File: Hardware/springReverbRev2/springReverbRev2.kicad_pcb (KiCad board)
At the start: 2 copper layers, 215 x 159.5 mm, 100 parts, among them IC102 TL074, IC103 TL074, J901 AudioJack2_SwitchT, J902 AudioJack2, J903 AudioJack2, J904 AudioJack2, J905 AudioJack2_SwitchT, J906 AudioJack2, J907 Conn_01x08_Socket, J908 Conn_01x08_Pin, J909 Conn_01x09_Socket, J910 Conn_01x09_Pin, J911 2_pin_Molex_header, J912 2_pin_Molex_header, SW901 SW_SPDT_MSM, U1 TL072, U2 TL072, U7 NE5532, U901 L78L05_TO92, X101 RCA, X102 RCA

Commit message: PCB revisions, Docs
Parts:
- added B901: Board, AO_tht:Board_Marker, F.Cu at (182.0, 28.5)
- added B902: Board, AO_tht:Board_Marker, F.Cu at (141.0, 28.5)
- C1, C101, C109, C2: footprint AO_tht:C_Disc_D3.0mm_W1.6mm_P2.50mm -> AO_tht:C_Radial_D8.0mm_H11.5mm_P3.50mm
- C108, C110, C3, C4: footprint AO_tht:C_Disc_D3.0mm_W1.6mm_P2.50mm -> AO_tht:C_Rect_L7.2mm_W2.5mm_P5.00mm_FKS2_FKP2_MKS2_MKP2
- moved C109 11.5 mm to (195.2, 117.8), turned to 180 degrees
- moved C110 5.12 mm to (194.0, 105.1)
- moved X101 3.38 mm to (247.3, 118.2)
- moved X102 3.38 mm to (265.1, 118.2)
- moved C101 2.87 mm to (251.1, 135.2)
- moved C4 2.50 mm to (215.6, 74.5)
- moved C108 2.46 mm to (230.8, 129.3)
- moved C1 1.27 mm to (200.3, 131.8)
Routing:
- net Net-(C109-Pad1): track 8.45 -> 20.3 mm
- net Net-(IC102B--): track 27.5 -> 34.3 mm
- net /Back board/TO_TANK: track 128.0 -> 133.7 mm
- net /Back board/MIXPOT_WET_B: track 81.8 -> 84.4 mm
- net /Back board/TRIM_B: track 22.8 -> 24.7 mm
- net /Back board/TO_TANK_S_B: track 126.3 -> 128.1 mm
- net /Back board/AUDIO_IN_2: track 116.0 -> 114.3 mm
- net /Back board/IN_1: track 40.4 -> 38.8 mm
- net +12V: track 161.4 -> 162.5 mm
- net /Back board/EQ_POT_3_B: track 46.3 -> 45.3 mm
- net /Back board/EQ_POT_1_B: track 41.1 -> 42.2 mm
- net /Back board/IN_2: track 9.74 -> 8.74 mm
- net /Front board/AUDIO_IN_1: track 50.1 -> 51.1 mm
- net /Back board/XFADE: track 57.8 -> 58.7 mm
- net /Back board/REVERB_RETURN: track 111.3 -> 110.7 mm
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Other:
- board text added: "Circuit design by Tom Whitwell CC-BY-SA"
- board text added: "FROM/GND"
- board text added: "Kosmo layout by Rich Holmes Mar 2023"
- board text added: "TO/GND"
- board text added: "https://github.com/TomWhitwell/Spring-Reverb-Mk-2"
- board text removed: "Circuit design by Tom Whitwell https://github.com/TomWhitwell/Spring-Reverb-Mk-2 CC-BY-SA"
- board text removed: "Kosmo layout by Rich Holmes Feb 2022"

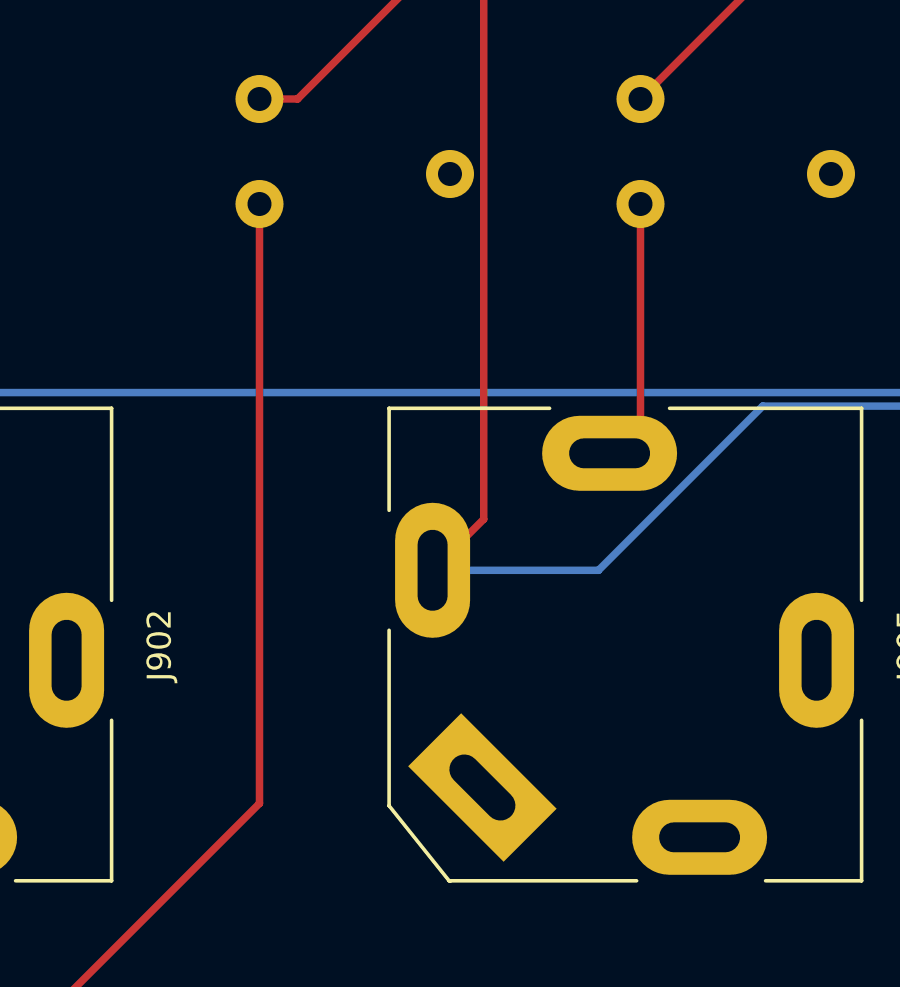
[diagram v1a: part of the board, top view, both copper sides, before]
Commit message: Restore R4 and R5 references; change C1 and C2 values; mark R5 to omit; README list of changes
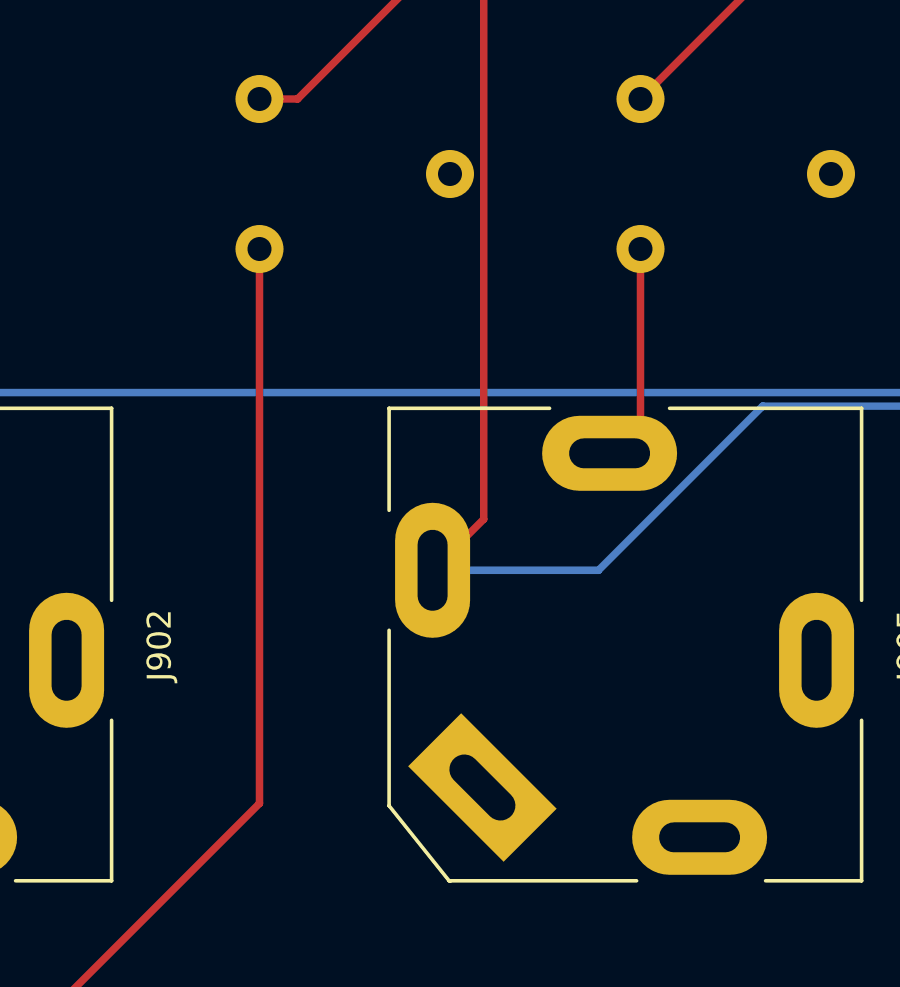
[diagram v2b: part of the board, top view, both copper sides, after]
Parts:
- C1, C2: value 10uF -> 1uF; footprint AO_tht:C_Radial_D8.0mm_H11.5mm_P3.50mm -> AO_tht:C_Rect_L7.2mm_W7.2mm_P5.00mm_FKS2_FKP2_MKS2_MKP2
- renumbered R901 to R4, R902 to R5
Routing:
- net /Back board/IN_2: track 8.74 -> 7.24 mm
- net /Back board/IN_1: track 38.8 -> 37.3 mm
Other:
- board text added: "OMIT?"

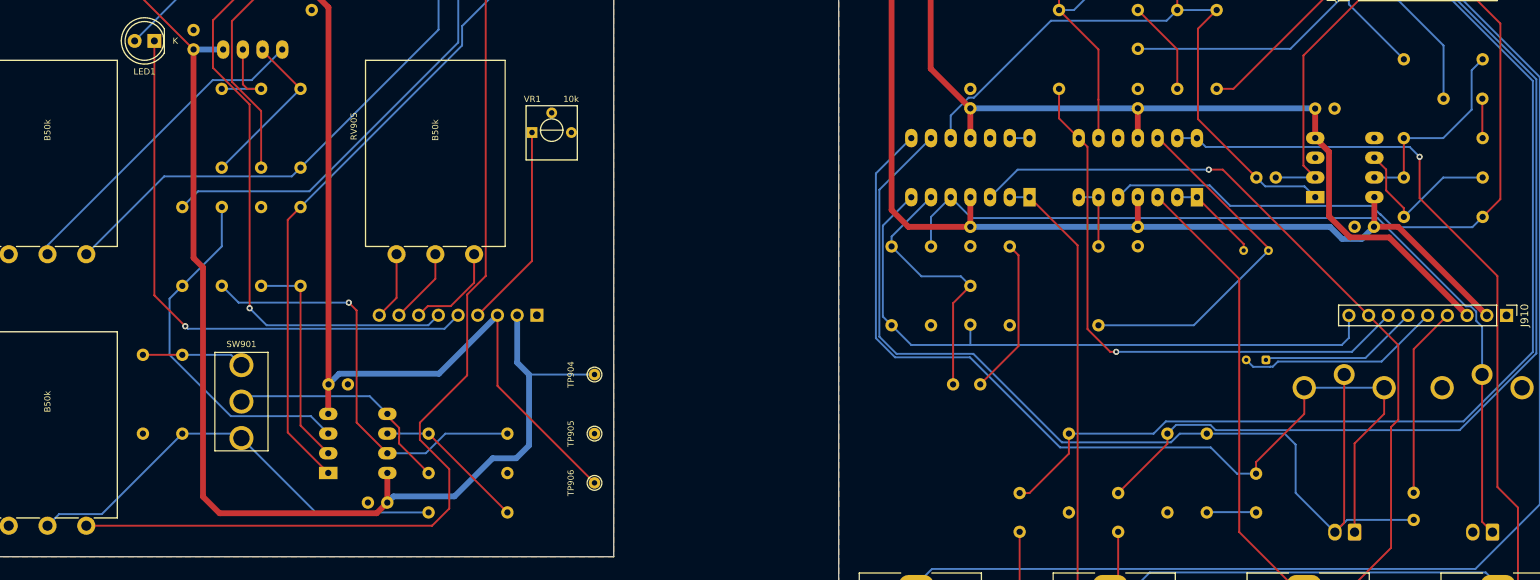
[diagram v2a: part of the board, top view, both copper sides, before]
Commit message: Docs; make LED position consistent
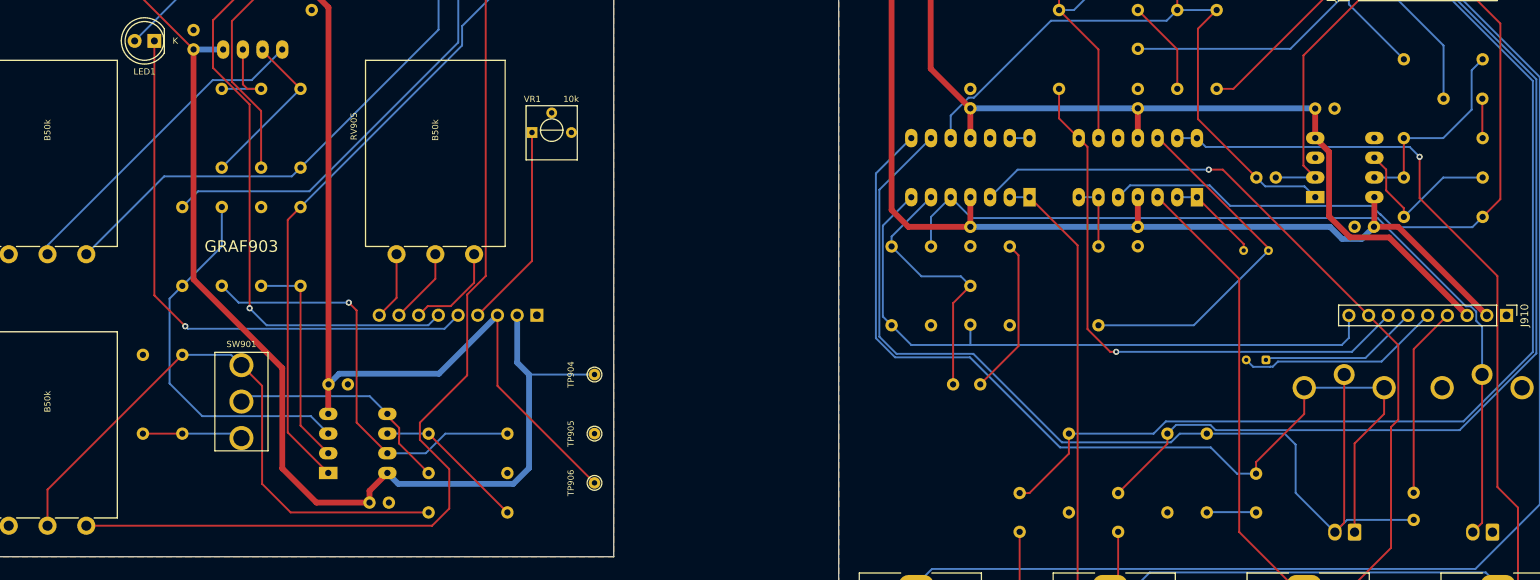
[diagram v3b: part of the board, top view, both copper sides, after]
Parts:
- added GRAF903: Holes, springreverb:springreverb_panel_holes2, F.Cu at (100.0, 100.0)
- moved R25 10.2 mm to (87.3, 124.1), turned to 90 degrees
- moved R26 10.2 mm to (92.4, 114.0), turned to -90 degrees
- moved C903 2.29 mm to (116.5, 133.0), turned to 0 degrees
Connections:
- net /Back board/MIXPOT_DRY_B renamed /Back board/MIXPOT_BRICK_B
- net /Back board/MIXPOT_WET_B renamed /Back board/MIXPOT_SPRING_B
- net /Front board/MIXPOT_DRY_F renamed /Front board/MIXPOT_BRICK_F
- net /Front board/MIXPOT_MIX_F renamed /Front board/MIXPOT_SB_MIX_F
- net /Front board/MIXPOT_WET_F renamed /Front board/MIXPOT_SPRING_F
- J907 pad 8: unconnected-(J907-Pin_8-Pad8) -> GND
- J908 pad 8: unconnected-(J908-Pin_8-Pad8) -> GND_B
- J912 pad 1: /Back board/FROM_TANK -> GND_B
- J912 pad 2: GND_B -> /Back board/FROM_TANK
- R25 pad 1: /Front board/FB_ON -> Net-(R25-Pad1)
- R26 pad 2: /Front board/FB_ON -> Net-(R25-Pad1)
- SW901 pad 1: /Front board/FB_LEVEL -> Net-(R25-Pad1)
- SW901 pad 3: /Front board/FB_ON -> /Front board/FB_LEVEL
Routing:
- net /Front board/FB_LEVEL: track 58.3 -> 76.8 mm
- net /Front board/FB_ON: track 13.3 -> 0.00 mm
- net Net-(R25-Pad1): track 0.00 -> 12.9 mm
- net +12V: track 162.5 -> 153.2 mm
- net Net-(U1A-+): track 46.5 -> 48.7 mm
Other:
- board text added: "GND/FROM"
- board text added: "Kosmo layout by Rich Holmes April 2023"
- board text added: "TO SLV/TIP"
- board text removed: "FROM/GND"
- board text removed: "Kosmo layout by Rich Holmes Mar 2023"
- board text removed: "TO/GND"

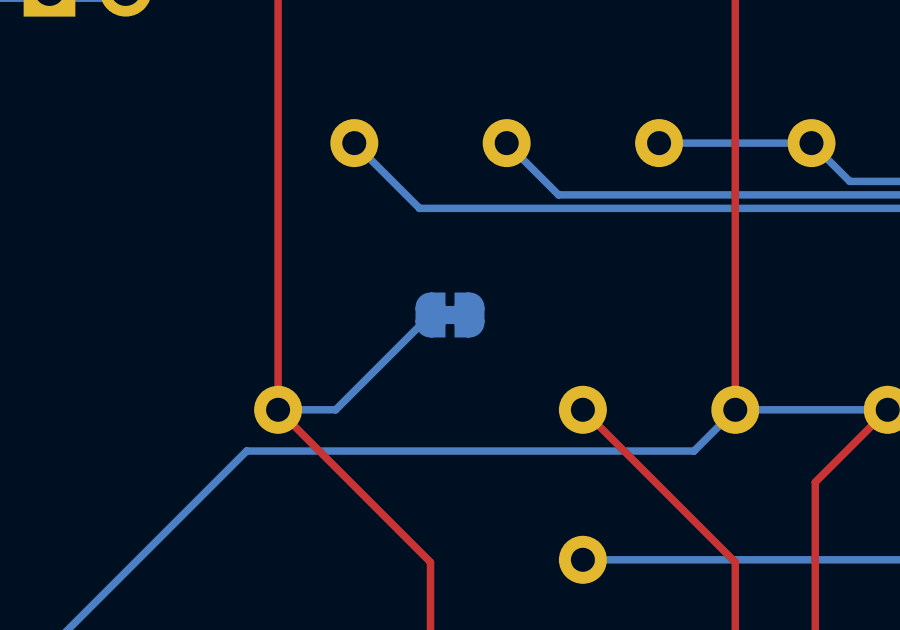
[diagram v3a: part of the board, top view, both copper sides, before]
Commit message: Use open not bridged jumper
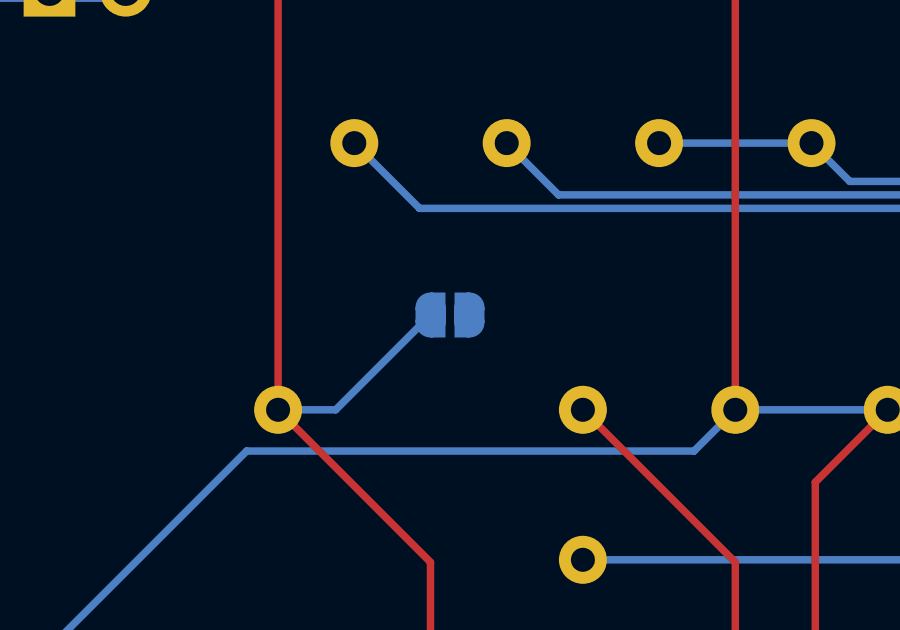
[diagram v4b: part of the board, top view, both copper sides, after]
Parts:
- SJ101: footprint Jumper:SolderJumper-2_P1.3mm_Bridged_RoundedPad1.0x1.5mm -> Jumper:SolderJumper-2_P1.3mm_Open_RoundedPad1.0x1.5mm
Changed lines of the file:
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@@
     )
   )
-  (footprint "Jumper:SolderJumper-2_P1.3mm_Bridged_RoundedPad1.0x1.5mm" (layer "B.Cu")
+  (footprint "Jumper:SolderJumper-2_P1.3mm_Open_RoundedPad1.0x1.5mm" (layer "B.Cu")
     (at 211.14 66.36 180)
-    (descr "SMD Solder Jumper, 1x1.5mm, rounded Pads, 0.3mm gap, bridged with 1 copper strip")
-    (tags "net tie solder jumper bridged")
+    (descr "SMD Solder Jumper, 1x1.5mm, rounded Pads, 0.3mm gap, open")
+    (tags "solder jumper open")
     (property "Manufacturer" "")
     (property "Part" "")
@@
     (property "ki_keywords" "solder jumper SPST")
     (attr exclude_from_pos_files exclude_from_bom)
-    (net_tie_pad_groups "1, 2")
     (fp_text reference "SJ101" (at 0 1.8) (layer "B.SilkS")
         (effects (font (size 1 1) (thickness 0.15)) (justify mirror))
@@
         (effects (font (size 1 1) (thickness 0.15)) (justify mirror))
     )
-    (fp_poly
-      (pts
-        (xy 0.25 0.3)
-        (xy -0.25 0.3)
-        (xy -0.25 -0.3)
-        (xy 0.25 -0.3)
-      )
-      (stroke (width 0) (type solid)) (fill solid) (layer "B.Cu"))
     (fp_line (start -1.4 -0.3) (end -1.4 0.3)
       (stroke (width 0.12) (type solid)) (layer "B.SilkS"))
